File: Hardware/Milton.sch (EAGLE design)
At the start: 83 parts, among them Q1 12MHz, U1 FT231X, U10 SI4464, U3 USD-SOCKETNEW, U4 DDC113TU-7-F, U5 TPS61200, U6 TCR2EE50,LM, U7 MMA8452Q, U8 MAX31850K, U9 BME280, X1 B4B-ZR, X2 M023.5MM, X3 SMA003.062

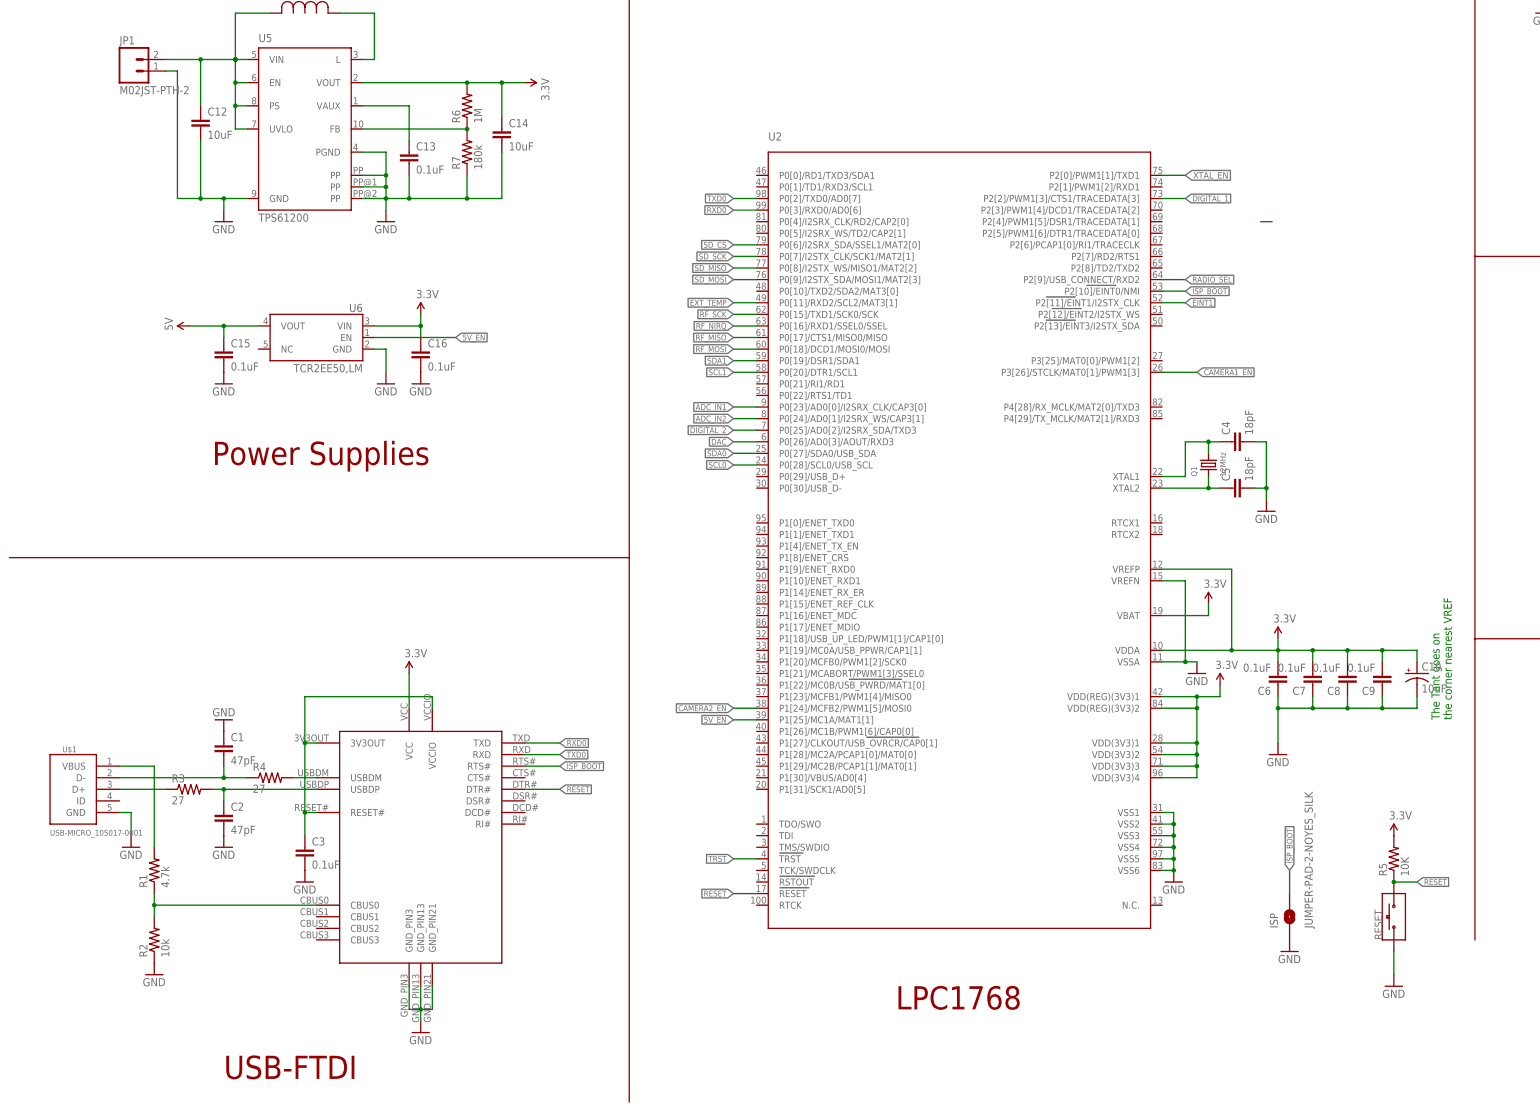
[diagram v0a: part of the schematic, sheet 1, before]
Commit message: Update
Removed FTDI from board. Added tx/rx header and isp button

Adjusted gps antenna position
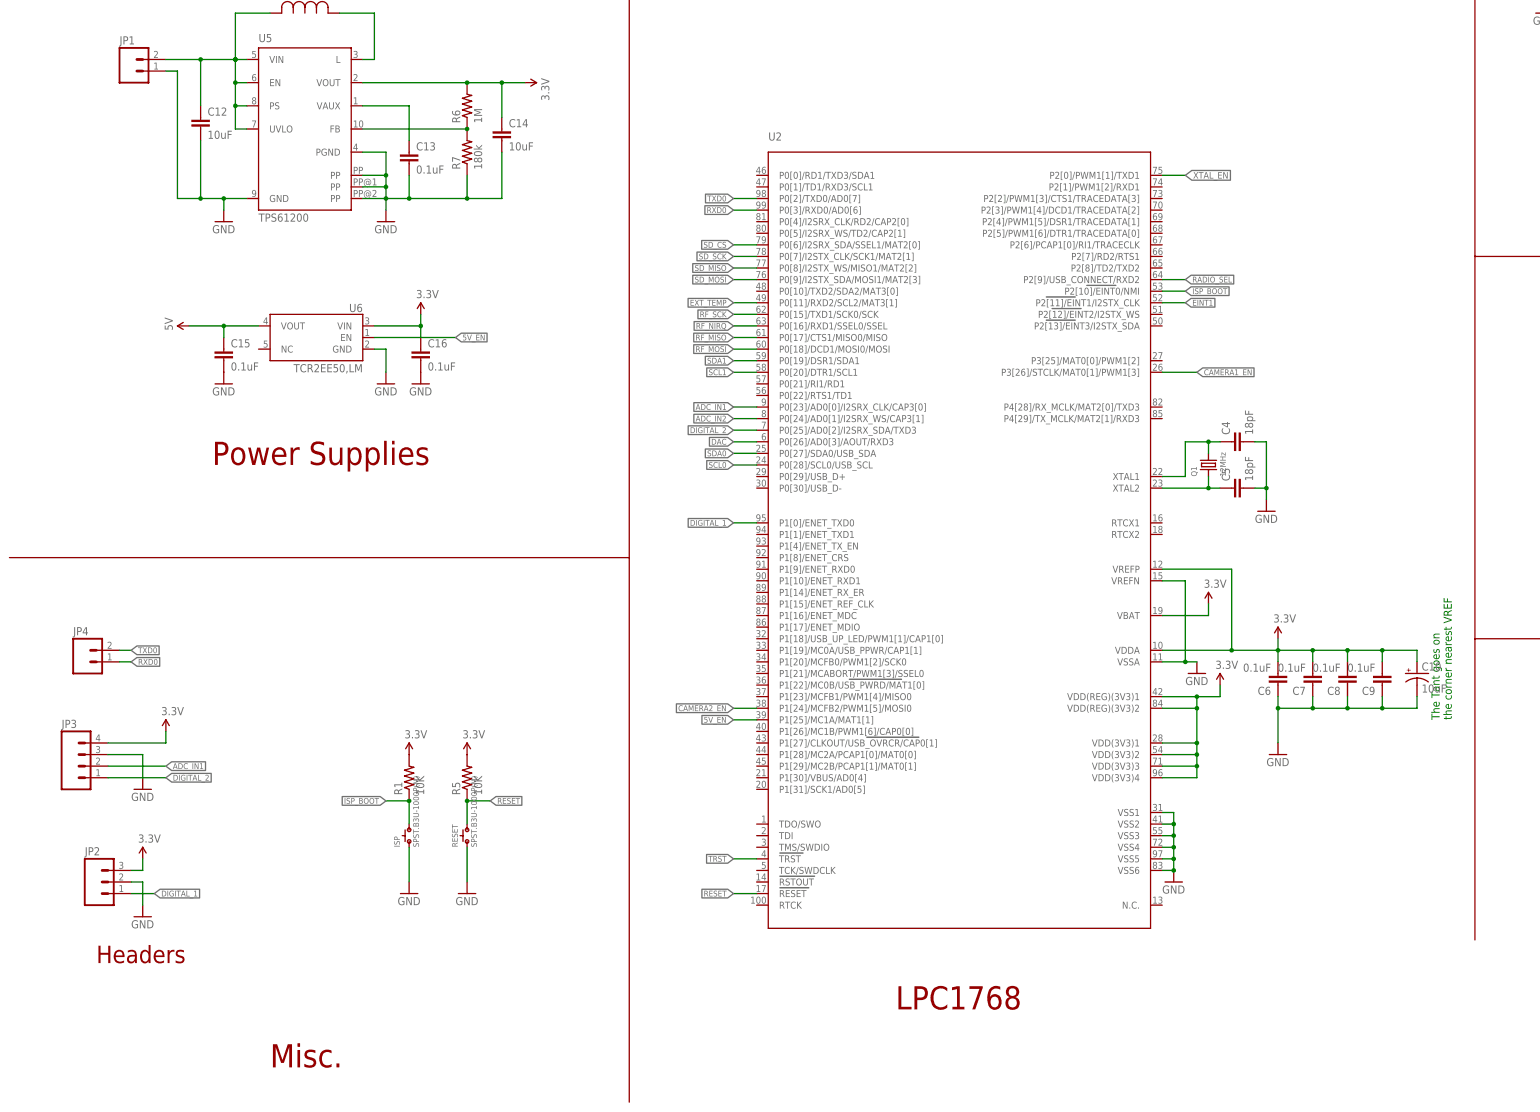
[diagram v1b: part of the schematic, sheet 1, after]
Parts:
- removed C1, C2: 47pF, SparkFun-Capacitors:CAP0603-CAP
- removed C3: 0.1uF, SparkFun-Capacitors:CAP0603-CAP
- removed R2: 10k, SparkFun-Resistors:RESISTOR0603
- removed R3, R4: 27, SparkFun-Resistors:RESISTOR0603
- removed U$1: USB-MICRO_105017-0001, wrea:USB-MICRO_105017-0001
- removed U1: FT231X, wrea:FT231X
- added JP4: (no value), SparkFun-Connectors:M02LOCK
- ISP: value JUMPER-PAD-2-NOYES_SILK -> SPST.B3U-1000P(M); device SparkFun-Passives:JUMPER-PAD-2-NOYES_SILK -> omron:SPST.B3U-1000P(M)
- JP1: value M02JST-PTH-2 -> (none)
- R1: value 4.7k -> 10K; MPN ESR03EZPJ472 -> ESR03EZPJ103
- RESET: value SWITCH -> SPST.B3U-1000P(M); device notes-arducorder-mini:SWITCH -> omron:SPST.B3U-1000P(M); MPN KMT071 NGJ LHS -> (none)
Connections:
- removed net N$10: R1.2, U$1.VBUS
- removed net N$12: C3.1, U1.3V3OUT, U1.RESET#, U1.VCCIO
- removed net N$21: R1.1, R2.2, U1.CBUS0
- removed net N$4: C2.1, R3.2, U1.USBDP
- removed net N$5: R4.2, U1.USBDM
- removed net N$7: R3.1, U$1.D+
- removed net N$9: C1.2, R4.1, U$1.D-
- net 3.3V: now also R1.2; no longer U1.VCC
- net DIGITAL_1: now also U2.P1[0]/ENET_TXD0; no longer U2.P2[2]/PWM1[3]/CTS1/TRACEDATA[3]
- net GND: now also RESET.1; no longer C1.1, C2.2, C3.2, R2.1, RESET.1A, U$1.GND, U1.GND_PIN13, U1.GND_PIN21, U1.GND_PIN3
- net ISP_BOOT: now also R1.1; no longer U1.RTS#
- net RESET: now also RESET.2; no longer RESET.2A, U1.DTR#
- net RXD0: now also JP4.1; no longer U1.TXD
- net TXD0: now also JP4.2; no longer U1.RXD
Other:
- note added: "Misc."
- note removed: "USB-FTDI"
- moved on the sheet: C20, C35, FB1, FB2, R1, R5, U8, X2
